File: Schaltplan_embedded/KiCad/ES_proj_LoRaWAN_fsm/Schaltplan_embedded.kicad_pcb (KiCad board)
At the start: 2 copper layers, 78 parts, among them IC1 TPS22943DCKR, IC2 BGA824N6E6327XTSA1, IC3 TESEO-LIV3F, IC4 L6924D, IC5 SPV1040T, IC6 TLS850B0TBV33ATMA1, IC7 TLS850B0TBV55ATMA1, J1 Conn_02x05_Odd_Even, J2 Conn_01x02, J3 53048-0810, J4 CONSMA002-L-G, J5 CONSMA002-L-G, J6 CON-SOCJ-2155, J7 Conn_01x02, U1 STM32L476RGTx, U2 RFM92W_93W, Y1 Crystal 8Mhz

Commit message: Neue platine
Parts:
- moved J4 84.6 mm to (185.0, 109.0), turned to 0 degrees
- moved J3 48.7 mm to (141.0, 112.8), turned to 0 degrees
- moved C23 39.1 mm to (156.3, 55.2)
- moved C18 37.4 mm to (112.0, 96.2), turned to 90 degrees
- moved R11 35.5 mm to (156.4, 52.9), turned to 180 degrees
- moved C19 35.2 mm to (108.0, 95.1), turned to 180 degrees
- moved D1 34.8 mm to (123.5, 97.2), turned to 0 degrees
- moved IC2 33.9 mm to (112.0, 86.5)
- moved C21 32.7 mm to (149.4, 59.7), turned to 270 degrees
- moved J7 32.6 mm to (156.5, 47.0)
- moved C9 32.3 mm to (186.0, 67.5), turned to 180 degrees
- moved R5 31.4 mm to (99.6, 103.2), turned to 90 degrees
- moved L2 30.7 mm to (104.8, 89.0), turned to 90 degrees
- moved IC4 30.2 mm to (150.7, 53.9), turned to 90 degrees
- moved C36 30.1 mm to (187.0, 76.0), turned to 270 degrees
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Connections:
- IC3 pad 13: (no net) -> AntOFF
- U1 pad 16: AntOFF -> (no net)
- U1 pad 40: LED_OUT -> (no net)
- U1 pad 9: (no net) -> LED_OUT
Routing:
- net +3V3: track 186.9 -> 280.7 mm, vias 2 -> 4
- net Net-(J4-Pad5): track 101.4 -> 10.6 mm, vias 1 -> 0
- net V_BAT: track 118.3 -> 77.0 mm, vias 3 -> 2
- net BAT_STAT2: track 80.5 -> 41.4 mm
- net BAT_STAT1: track 79.0 -> 43.4 mm
- net RF_IN: track 38.6 -> 5.37 mm
- net GND: track 28.5 -> 57.7 mm, vias 16 -> 20
- net UART_4_RX: track 45.6 -> 17.5 mm
- net UART_4_TX: track 45.1 -> 19.2 mm
- net Net-(C28-Pad1): track 10.8 -> 32.7 mm, vias 0 -> 2
- net LoRa_DI05: track 35.3 -> 14.1 mm, vias 2 -> 0
- net LoRa_RESET: track 33.0 -> 13.7 mm, vias 2 -> 0
- net LoRa_DI00: track 25.5 -> 44.1 mm
- net 5V_ENABLE: track 80.7 -> 63.1 mm
- net Net-(C11-Pad2): track 28.0 -> 10.9 mm, vias 1 -> 0
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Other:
- net class 3V3: trace_width 0.15 -> 0.4
- net class 5V: trace_width 0.15 -> 0.6
- net class Antenna added: clearance 0.15, trace_width 0.4, via_dia 0.9, via_drill 0.6
- net class Data: trace_width 0.1 -> 0.2
- net class Default: trace_width 0.1 -> 0.2
- rule trace_min: 0.1 -> 0.2
- board text added: "Feinstaubmessung: Gallego, Lutkenhaus, Kompalla, Vega, Hamsen, Wolters"

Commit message: git :)
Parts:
- removed the C11 at (102.2, 89.0)
- removed the C19 at (108.0, 95.1)
- removed the C20 at (112.0, 78.5)
- removed FL1: B4327, SamacSys_Parts:B39162B4353P810
- removed the IC2 at (112.0, 86.5)
- removed the R4 at (103.6, 103.0)
- added C9: 120pF, Capacitor_SMD:C_0805_2012Metric_Pad1.15x1.40mm_HandSolder, F.Cu at (181.2, 104.5)
- C12: value 3.9pF -> 120pF; footprint Capacitors_SMD:C_0805 -> Capacitor_SMD:C_0805_2012Metric_Pad1.15x1.40mm_HandSolder
- C13: value 10nF -> 1uF; footprint Capacitors_SMD:C_0805 -> Capacitor_SMD:C_0805_2012Metric_Pad1.15x1.40mm_HandSolder
- C14: value 1uF -> 2.2uF; footprint Capacitors_SMD:C_0805 -> Capacitor_SMD:C_0805_2012Metric_Pad1.15x1.40mm_HandSolder
- C15, C16, C17: footprint Capacitors_SMD:C_0805 -> Capacitor_SMD:C_0805_2012Metric_Pad1.15x1.40mm_HandSolder
- C18: value 1nF -> 10nF; footprint Capacitors_SMD:C_0805 -> Capacitor_SMD:C_0805_2012Metric_Pad1.15x1.40mm_HandSolder
- L1, L3, L4: footprint Resistors_SMD:R_0805_HandSoldering -> Inductor_SMD:L_0805_2012Metric_Pad1.15x1.40mm_HandSolder
- L2: value 6.8nH -> 100nH; footprint Resistors_SMD:R_0805_HandSoldering -> Inductor_SMD:L_0805_2012Metric_Pad1.15x1.40mm_HandSolder
- Y1: value Crystal 8Mhz -> ECS-80-12-30Q-DS-TR; footprint Crystals:Crystal_SMD_HC49-SD_HandSoldering -> myLib:Quarz
- moved C13 36.5 mm to (105.0, 87.5), turned to 180 degrees
- moved C18 34.8 mm to (139.0, 74.2), turned to 0 degrees
- moved L2 20.3 mm to (125.0, 87.5), turned to 180 degrees
- moved D2 15.9 mm to (111.0, 80.8)
- moved L1 15.4 mm to (113.2, 81.5)
- moved C12 12.9 mm to (113.5, 77.8), turned to 180 degrees
- moved R4 9.68 mm to (104.8, 95.0)
- moved C2 7.90 mm to (129.0, 94.0)
- moved IC1 7.69 mm to (110.2, 90.8)
- moved C14 7.40 mm to (110.0, 95.8), turned to 0 degrees
- moved C11 7.11 mm to (104.2, 90.5), turned to 180 degrees
- moved J3 5.90 mm to (136.2, 109.2)
- moved C16 5.35 mm to (133.2, 82.2)
- moved J4 5.15 mm to (187.5, 104.5)
- moved J5 4.99 mm to (104.8, 77.8)
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- renumbered C9 to C10, C10 to C11, C21 to C19, C22 to C20, C23 to C21, C24 to C22, C25 to C23, C26 to C24, C27 to C25, C28 to C26, C29 to C27, C30 to C28, C31 to C29, C32 to C30, C33 to C31, C34 to C32, C35 to C33, C36 to C34, C37 to C35, IC3 to IC2, IC4 to IC3, IC5 to IC4, IC6 to IC5, IC7 to IC6, R11 to R10, R12 to R11, R13 to R12, R14 to R13, R15 to R14, R5 to R4, R6 to R5, R7 to R6, R8 to R7, R9 to R8, R10 to R9
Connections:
- net AntOFF renamed Net-(IC1-Pad4)
- C11 pad 1: Net-(C10-Pad1) -> Net-(C11-Pad1)
- C12 pad 1: GND -> Net-(C12-Pad1)
- C12 pad 2: Net-(C11-Pad1) -> Net-(C12-Pad2)
- C13 pad 1: +3V3 -> Net-(C11-Pad1)
- C14 pad 1: Net-(C10-Pad1) -> Net-(C14-Pad1)
- C15 pad 1: UART_5_RX -> UART_5_TX
- C16 pad 1: Net-(C16-Pad1) -> UART_5_RX
- C17 pad 1: UART_5_TX -> Net-(C17-Pad1)
- C18 pad 1: GND -> +3V3
- C18 pad 2: +3V3 -> GND
- D2 pad 1: Net-(C11-Pad2) -> Net-(C12-Pad2)
- IC1 pad 1: Net-(C10-Pad1) -> Net-(C11-Pad1)
- IC1 pad 5: +3V3 -> Net-(C14-Pad1)
- IC2 pad 1: GND -> Net-(IC2-Pad1)
- IC2 pad 11: RF_IN -> Net-(C12-Pad1)
- IC2 pad 6: Net-(C16-Pad1) -> Net-(C17-Pad1)
- IC2 pad 7: Net-(C16-Pad1) -> Net-(C17-Pad1)
- IC2 pad 8: Net-(C16-Pad1) -> Net-(C17-Pad1)
- J4 pad 1: GND -> Net-(C9-Pad2)
- J4 pad 5: Net-(J4-Pad5) -> GND
- J5 pad 1: GND -> Net-(C12-Pad2)
- J5 pad 5: Net-(C11-Pad2) -> GND
- L1 pad 1: Net-(C11-Pad2) -> Net-(C12-Pad2)
- L1 pad 2: Net-(C10-Pad1) -> Net-(C11-Pad1)
- L2 pad 1: Net-(C11-Pad1) -> Net-(IC2-Pad1)
- L2 pad 2: Net-(IC2-Pad5) -> GND
- L3 pad 2: Net-(C16-Pad1) -> Net-(C17-Pad1)
- R4 pad 1: +3V3 -> Net-(C14-Pad1)
- U2 pad 9: Net-(J4-Pad5) -> Net-(C9-Pad1)
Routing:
- net +3V3: track 280.7 -> 219.1 mm, vias 4 -> 0
- net Net-(IC1-Pad4): track 44.4 -> 14.7 mm
- net Net-(C14-Pad1): track 0.00 -> 18.8 mm, vias 0 -> 2
- net GND: track 57.7 -> 40.0 mm, vias 20 -> 37
- net +5V: track 89.3 -> 72.6 mm, vias 1 -> 3
- net JTAG_TDI: track 34.9 -> 20.9 mm, vias 3 -> 2
- net Net-(C10-Pad1): track 13.1 -> 0.00 mm
- net Net-(C12-Pad2): track 0.00 -> 12.8 mm
- net Net-(C11-Pad1): track 5.19 -> 17.0 mm
- net Net-(C11-Pad2): track 10.9 -> 0.00 mm
- net Net-(J4-Pad5): track 10.6 -> 0.00 mm
- net Net-(C17-Pad1): track 0.00 -> 10.3 mm
- net Net-(C16-Pad1): track 10.3 -> 0.00 mm
- net Net-(C2-Pad2): track 23.2 -> 13.9 mm
- net JTAG_TDO: track 19.5 -> 10.3 mm
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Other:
- net class Antenna: trace_width 0.4 -> 0.9
- board text added: "Feinstaubmessung: Gallego, Kompalla, Lütkenhaus, Vega, Hamsen, Wolters"
- board text added: "GPS"
- board text added: "LoRaWAN"
- board text added: "Reset"
- board text added: "Solar Zelle"
- board text removed: "Feinstaubmessung: Gallego, Lutkenhaus, Kompalla, Vega, Hamsen, Wolters"

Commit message: git fix attempt no. 10231931231410294124
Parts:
- moved C10 29.3 mm to (183.4, 96.7), turned to 90 degrees
- moved C8 26.5 mm to (185.9, 96.5), turned to 90 degrees
- moved C32 4.56 mm to (186.1, 68.7), turned to 180 degrees
- moved C1 4.06 mm to (135.2, 90.5), turned to 270 degrees
- moved C2 3.72 mm to (127.8, 90.5), turned to 270 degrees
- moved C18 2.02 mm to (137.0, 74.5)
- moved C4 1.75 mm to (151.7, 85.7), turned to 180 degrees
- moved Y1 1.44 mm to (129.0, 89.2)
- moved L2 1.30 mm to (123.7, 87.6)
- moved C24 0.51 mm to (159.3, 59.4)
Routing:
- net +5V: track 72.6 -> 98.5 mm, vias 3 -> 4
- net JTAG_TDO: track 10.3 -> 17.8 mm, vias 1 -> 2
- net SPI1_NSS: track 29.6 -> 23.6 mm
- net JTAG_TCK: track 17.6 -> 22.7 mm, vias 1 -> 0
- net V_BAT: track 75.2 -> 79.3 mm
- net Net-(C26-Pad1): track 32.7 -> 29.1 mm
- net 5V_ENABLE: track 60.6 -> 63.9 mm, vias 2 -> 6
- net USART_3_RX: track 17.4 -> 14.1 mm, vias 1 -> 0
- net V_SUPPLY: track 37.9 -> 40.8 mm, vias 2 -> 0
- net Net-(C14-Pad1): track 18.8 -> 16.1 mm
- net Net-(C2-Pad2): track 13.9 -> 12.1 mm
- net Net-(C1-Pad2): track 7.89 -> 6.14 mm
- net +3V3: track 219.1 -> 218.1 mm
- net UART_5_TX: track 29.3 -> 30.3 mm
- net Net-(IC2-Pad1): track 2.11 -> 2.95 mm
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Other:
- net class Data: clearance 0.1 -> 0.15
- net class Default: clearance 0.1 -> 0.15
- rule trace_clearance: 0.1 -> 0.15
- board text added: "JTAG"

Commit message: PCB decorations / Gerber Files
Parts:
- added REF**: MountingHole_2.2mm_M2_Pad_Via, MountingHole:MountingHole_2.2mm_M2_Pad_Via, F.Cu at (97.3, 105.0)
- added REF**: MountingHole_2.2mm_M2_Pad_Via, MountingHole:MountingHole_2.2mm_M2_Pad_Via, F.Cu at (97.3, 95.0)
- added REF**: MountingHole_2.2mm_M2_Pad_Via, MountingHole:MountingHole_2.2mm_M2_Pad_Via, F.Cu at (193.5, 65.0)
- added REF**: MountingHole_2.2mm_M2_Pad_Via, MountingHole:MountingHole_2.2mm_M2_Pad_Via, F.Cu at (193.5, 50.0)
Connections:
- IC5 pad 6: (no net) -> GND
- IC6 pad 6: (no net) -> GND
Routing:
- net GND: vias 51 -> 66
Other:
- board outline added: 105.2 x 70 mm

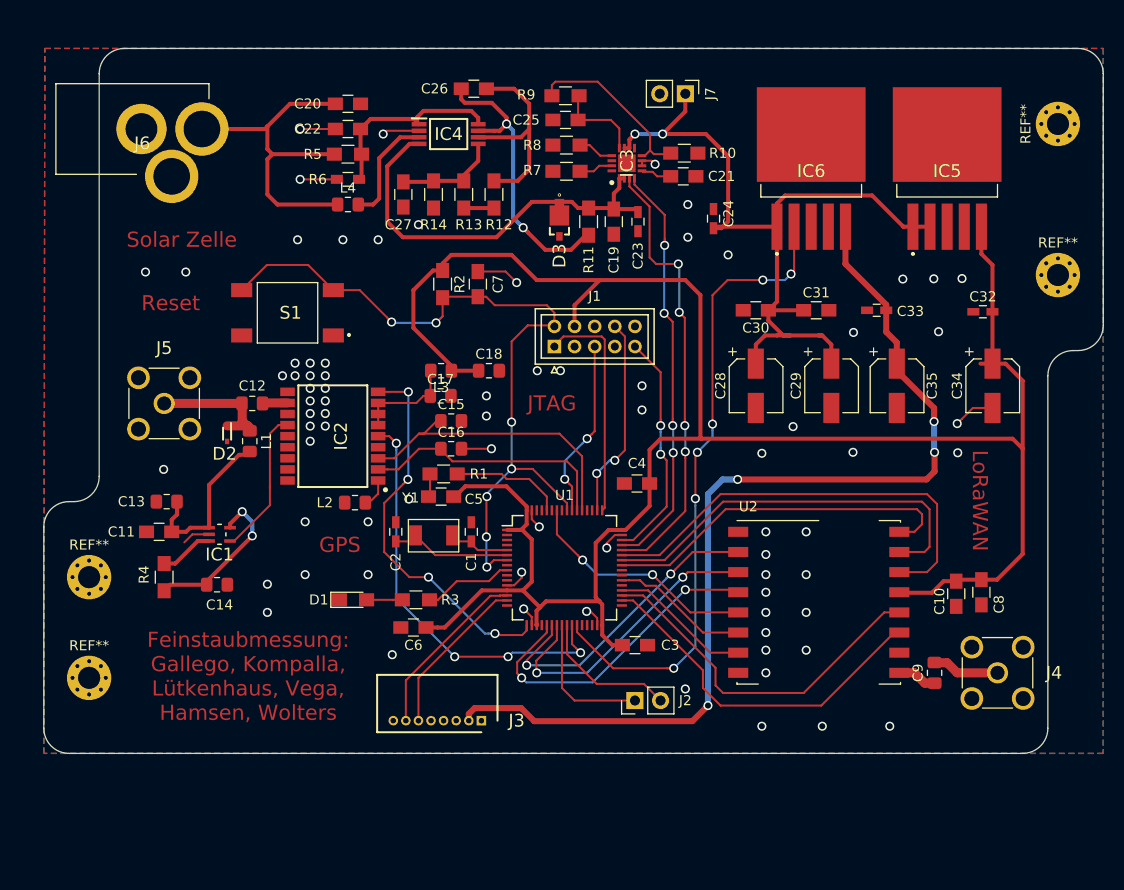
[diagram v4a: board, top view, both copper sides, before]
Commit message: Antenna conn change / layout fixes
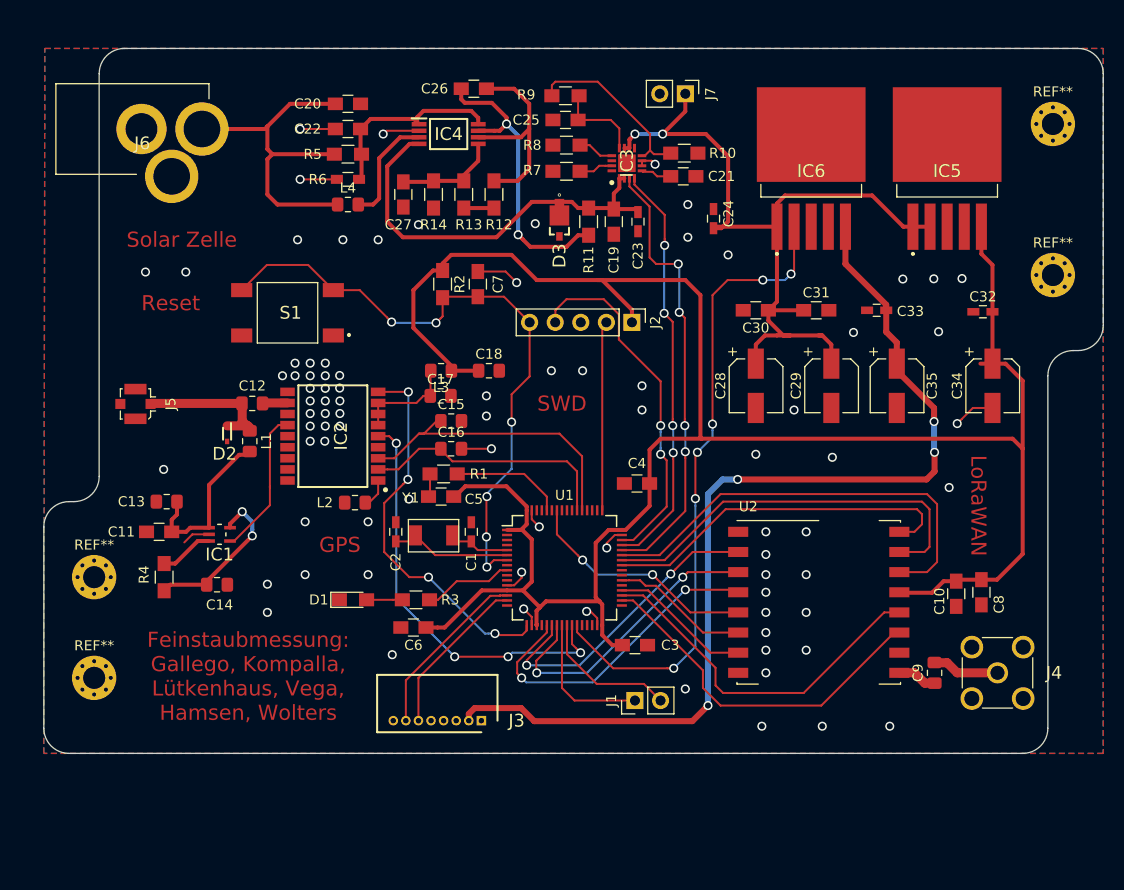
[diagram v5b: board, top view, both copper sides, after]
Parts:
- removed the REF** at (97.3, 105.0)
- removed the REF** at (97.3, 95.0)
- removed the REF** at (193.5, 65.0)
- removed the REF** at (193.5, 50.0)
- added REF**: MountingHole_2.2mm_M2_Pad_Via, MountingHole:MountingHole_2.2mm_M2_Pad_Via, F.Cu at (97.8, 95.0)
- added REF**: MountingHole_2.2mm_M2_Pad_Via, MountingHole:MountingHole_2.2mm_M2_Pad_Via, F.Cu at (97.8, 105.0)
- added REF**: MountingHole_2.2mm_M2_Pad_Via, MountingHole:MountingHole_2.2mm_M2_Pad_Via, F.Cu at (193.0, 65.0)
- added REF**: MountingHole_2.2mm_M2_Pad_Via, MountingHole:MountingHole_2.2mm_M2_Pad_Via, F.Cu at (193.0, 50.0)
- J1: value Conn_02x05_Odd_Even -> Conn_01x02; footprint Connectors_JAE:JAE_LY20-10P-2T_2x05x2.00mm_Straight -> Connector_PinHeader_2.54mm:PinHeader_1x02_P2.54mm_Vertical
- J2: value Conn_01x02 -> Conn_01x05; footprint Pin_Headers:Pin_Header_Straight_1x02_Pitch2.54mm -> Connector_PinHeader_2.54mm:PinHeader_1x05_P2.54mm_Vertical
- J5: value CONSMA002-L-G -> Conn_Coaxial; footprint SamacSys_Parts:CONSMA002LG -> Connector_Coaxial:U.FL_Molex_MCRF_73412-0110_Vertical
- moved J2 37.6 mm to (151.2, 69.7), turned to 270 degrees
- moved J1 36.0 mm to (151.5, 107.2), turned to 90 degrees
- moved J5 2.85 mm to (101.9, 77.8), turned to 90 degrees
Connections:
- net VREF renamed Net-(C25-Pad1)
- C7 pad 1: JTAG_RESET -> NRST
- J1 pad 1: JTAG_TCK -> USART_3_TX
- J1 pad 2: GND -> USART_3_RX
- J2 pad 1: USART_3_TX -> +3V3
- J2 pad 2: USART_3_RX -> SWCLK
- R2 pad 2: JTAG_RESET -> NRST
- S1 pad 3: JTAG_RESET -> NRST
- S1 pad 4: JTAG_RESET -> NRST
- U1 pad 46: JTAG_TMS -> SWDIO
- U1 pad 49: JTAG_TCK -> SWCLK
- U1 pad 50: JTAG_TDI -> (no net)
- U1 pad 55: JTAG_TDO -> (no net)
- U1 pad 56: JTAG_RESET -> (no net)
- U1 pad 7: JTAG_RESET -> NRST
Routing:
- net JTAG_RESET: track 77.4 -> 0.00 mm, vias 7 -> 0
- net NRST: track 0.00 -> 64.1 mm, vias 0 -> 6
- net SWDIO: track 0.00 -> 35.5 mm, vias 0 -> 2
- net JTAG_TMS: track 23.0 -> 0.00 mm, vias 2 -> 0
- net JTAG_TCK: track 22.7 -> 0.00 mm
- net JTAG_TDI: track 20.2 -> 0.00 mm, vias 2 -> 0
- net SWCLK: track 0.00 -> 18.8 mm
- net JTAG_TDO: track 17.8 -> 0.00 mm, vias 2 -> 0
- net Net-(C12-Pad2): track 12.8 -> 14.2 mm
- net GND: track 39.9 -> 40.2 mm, vias 66 -> 73
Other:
- board text added: "SWD"
- board text removed: "JTAG"

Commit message: Stecker gedreht
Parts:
- moved J3 9.03 mm to (127.9, 105.8), turned to 180 degrees
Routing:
- net +5V: track 98.5 -> 104.7 mm
- net UART_4_RX: track 16.2 -> 11.1 mm
- net UART_4_TX: track 17.5 -> 14.6 mm, vias 0 -> 2
- net GPS_WAKEUP: track 41.4 -> 40.2 mm
